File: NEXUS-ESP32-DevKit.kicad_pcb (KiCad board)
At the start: 2 copper layers, 28 x 55 mm, 25 parts, among them J1 USB_C_Receptacle_USB2.0_16P, J2 Conn_01x14_Pin, J3 Conn_01x10_Pin, Q1 Q_NPN_BCE, Q2 Q_NPN_BCE, SW1 SW_Push, SW2 SW_Push, U1 ESP32-WROOM-32E, U2 AMS1117-3.3, U3 CH340C

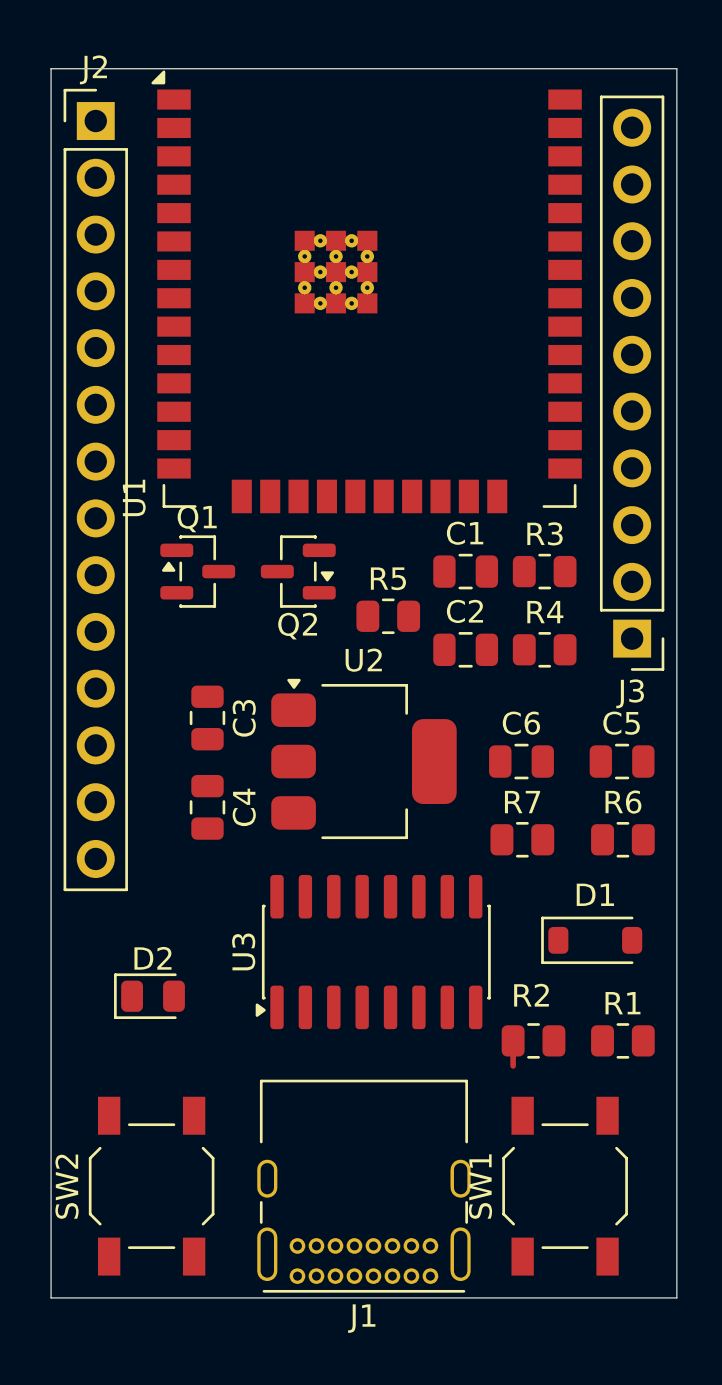
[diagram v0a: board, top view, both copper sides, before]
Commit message: Ruteo de senales y plano de tierra en B.Cu (pendiente vias de GND)
Avance en el ruteo del PCB del NEXUS-ESP32-DevKit:

- Se rutearon todas las señales de datos y alimentación en F.Cu:
  USB D+/D- (unificando pines duplicados A6/B6 y A7/B7 del conector
  USB-C), señales CC1/CC2, alimentación VBUS/+3V3, UART (TX/RX),
  auto-reset (DTR/RTS), y todas las conexiones a headers GPIO
- Se resolvieron zonas de alta congestión alrededor del conector
  USB-C mediante reducción puntual de ancho de pista y uso de vías
  para escape por la capa inferior
- Se creó el plano de tierra (zona de relleno) en la capa B.Cu,
  asignado a la red GND, cubriendo toda el área de la placa

Pendiente: colocar las vías de conexión entre los pads GND de los
componentes SMD (capa F.Cu) y el plano de tierra (B.Cu). Los pads
SMD existen únicamente en la capa superior, por lo que requieren
vías para alcanzar el plano inferior. Los pads THT de los headers
(J2/J3) conectan directamente al atravesar ambas capas.

Próximo paso: vías de GND, verificación final con DRC.
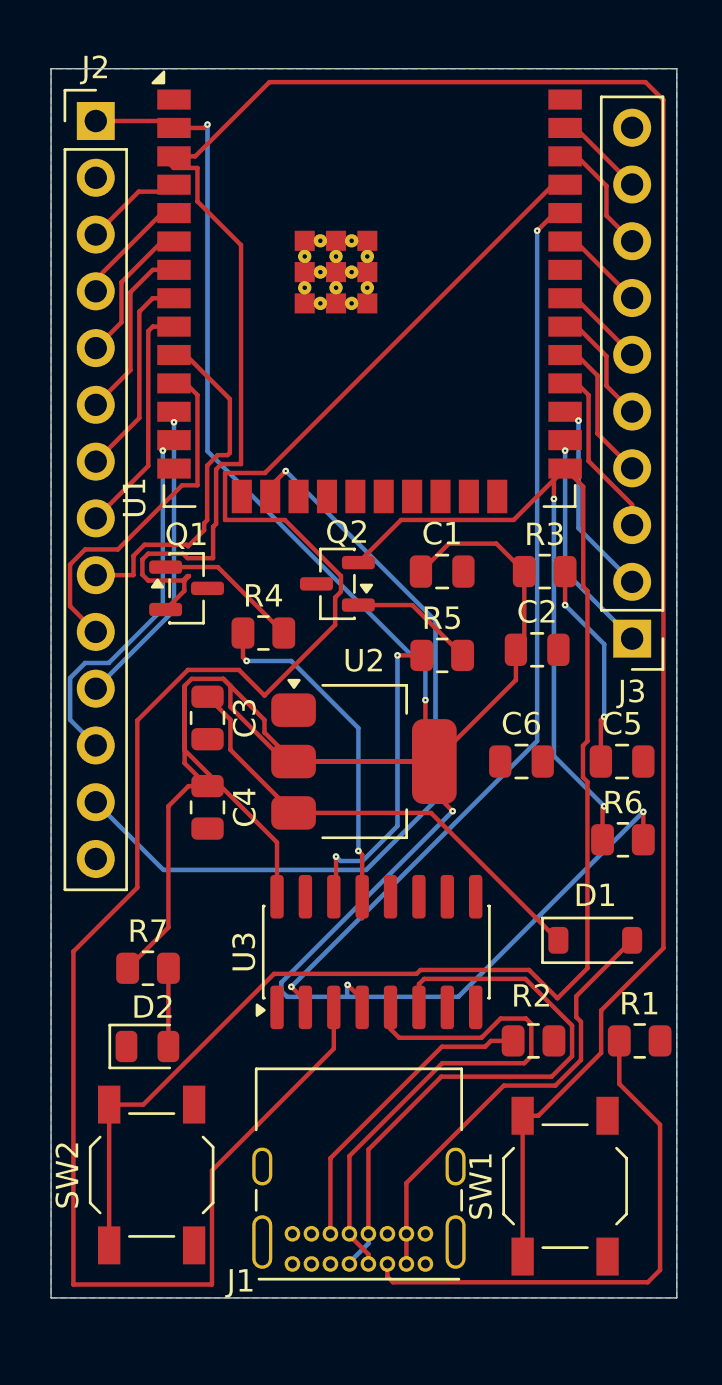
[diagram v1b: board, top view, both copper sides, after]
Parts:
- moved R7 17.7 mm to (107.3, 77.2)
- moved R4 12.6 mm to (112.5, 62.2)
- moved C2 3.20 mm to (124.8, 63.0)
- moved R5 2.98 mm to (120.5, 63.2)
- moved D2 2.26 mm to (107.3, 80.8)
- moved Q2 1.83 mm to (115.8, 60.0)
- moved C1 1.05 mm to (120.5, 59.5)
- moved Q1 0.90 mm to (109.1, 60.2)
- moved R1 0.75 mm to (129.3, 80.5)
- moved J1 0.59 mm to (119.8, 90.5)
- moved SW2 0.50 mm to (107.5, 86.5)
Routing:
- net +3V3: track 0.00 -> 141.2 mm, vias 0 -> 5
- net EN: track 0.00 -> 117.5 mm, vias 0 -> 2
- net TX: track 0.00 -> 90.0 mm
- net GPIO0: track 0.00 -> 83.5 mm, vias 0 -> 2
- net RX: track 0.00 -> 41.1 mm, vias 0 -> 2
- net IO13: track 0.00 -> 36.7 mm, vias 0 -> 1
- net D-: track 0.00 -> 26.5 mm, vias 0 -> 1
- net D+: track 0.00 -> 24.5 mm
- net Net-(J1-CC1): track 0.00 -> 24.1 mm
- net VBUS: track 0.00 -> 21.0 mm
- net Net-(D1-A): track 0.00 -> 20.2 mm
- net IO14: track 0.00 -> 16.7 mm, vias 0 -> 1
- net IO25: track 0.00 -> 16.2 mm
- net DTR: track 0.00 -> 16.2 mm, vias 0 -> 2
- net IO26: track 0.00 -> 16.1 mm
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- added copper zone on B.Cu, net GND

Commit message: Layout de PCB completo y verificado: DRC sin errores. Correccion de orientacion de headers J2/J3 (flip a cara inferior)
Se completó el ruteo y la verificación final del PCB del NEXUS-ESP32-DevKit:

- Vías de conexión a plano de tierra colocadas para todos los pads GND
  de componentes SMD (los pads THT de headers y conector conectan
  directamente al atravesar ambas capas)
- Plano de tierra (B.Cu) verificado y continuo tras reorganización
  de pistas
- Ajustes en reglas de diseño para compatibilidad con los footprints
  reales: margen mínimo reducido a 0.15mm (pitch fino del conector
  USB-C) y agujero pasante mínimo a 0.2mm (vías térmicas del pad
  central del ESP32-WROOM-32E) — ambos valores dentro de capacidades
  estándar de fabricación
- R1 reposicionada para respetar el margen mínimo al borde de placa
  (0.5mm)
- Pads GND B1/B12 del conector USB-C reforzados con pistas directas
  adicionales (alivio térmico incompleto resuelto)
- DRC final: 0 errores. Avisos restantes (serigrafía y proximidad
  de microvías en zona del conector) evaluados y aceptados como
  no bloqueantes para prototipo
Se detectó en el visor 3D que los pin headers J2/J3 quedaron con los
pines apuntando hacia arriba. Se voltearon (flip) a la cara inferior
para que los pines sobresalgan por debajo de la placa, permitiendo
montarla en protoboard como una DevKit comercial. DRC re-verificado:
0 errores.
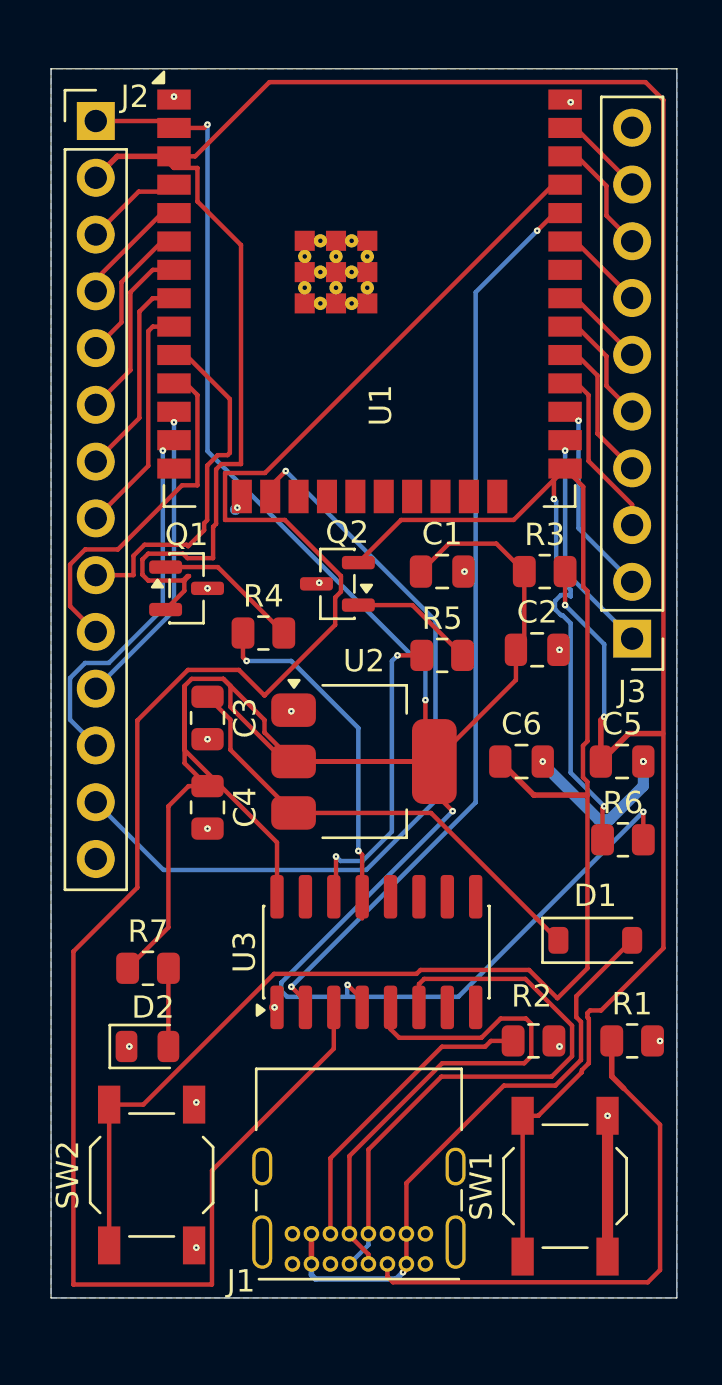
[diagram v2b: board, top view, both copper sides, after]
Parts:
- moved R1 0.34 mm to (129.0, 80.5)
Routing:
- net GND: track 0.00 -> 16.2 mm, vias 0 -> 20
- net EN: track 117.5 -> 125.1 mm
- net Net-(D1-A): track 20.2 -> 26.8 mm, vias 0 -> 1
- net GPIO0: track 83.5 -> 89.0 mm
- net D-: track 26.5 -> 26.6 mm, vias 1 -> 0

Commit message: Serigrafia: etiquetado de pinout en ambas caras
Se agregó el etiquetado de pines (pinout) de los headers J2 y J3 en
la serigrafía, en ambas caras de la placa (F.Silkscreen y B.Silkscreen):

- Cara superior: legible con la placa montada en protoboard
- Cara inferior: legible al inspeccionar la placa por debajo
- Tamaño de texto 0.7mm con grosor 0.12mm, dentro de los límites
  de fabricación estándar para serigrafía legible

Con esto la placa queda visualmente completa y lista para generar
los archivos de fabricación.
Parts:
- J2, J3: moved to B.Cu
- turned J2 to 180 degrees
- turned J3 to 0 degrees
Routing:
- net GND: track 16.2 -> 19.2 mm, vias 20 -> 22
- net Net-(D1-A): vias 1 -> 0
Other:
- board text added: "04"
- board text added: "05"
- board text added: "13"
- board text added: "14"
- board text added: "16"
- board text added: "17"
- board text added: "18"
- board text added: "19"
- board text added: "21"
- board text added: "22"
- board text added: "23"
- board text added: "25"
- board text added: "26"
- board text added: "27"
- board text added: "32"
- board text added: "33"
- board text added: "34"
- board text added: "35"
- board text added: "36"
- board text added: "39"
- board text added: "3V3"
- board text added: "EN"
- board text added: "GND"
